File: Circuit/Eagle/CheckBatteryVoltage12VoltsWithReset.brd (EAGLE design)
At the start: 100.3 x 70 mm, 75 parts

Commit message: Aggiunte per regolazione piu precisa.
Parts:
- added E$76: W203, rcl:RTRIM3296W
- added E$77, E$79: zener 12v, ref-packages-longpad:ZDIO-7.5
- added E$78: 1k, eagle-ltspice:0204/7
- added E$80: w501, rcl:RTRIM3296W
- added E$81: zener 4.3v, ref-packages-longpad:ZDIO-7.5
- added E$82: 100, eagle-ltspice:0204/7
- E$10: value zener 12v -> zener 10v
- E$11: value 1k -> 680
- moved E$38 32.0 mm to (98.3, 67.5)
- moved E$66 29.1 mm to (98.7, 53.2)
- moved E$39 28.0 mm to (98.6, 56.6)
- moved E$67 27.0 mm to (98.4, 49.9)
- moved E$68 26.0 mm to (98.3, 60.2)
- moved E$75 24.0 mm to (98.2, 63.7)
- moved E$49 15.9 mm to (26.6, 19.2)
- moved E$10 15.9 mm to (30.9, 43.0)
- moved E$13 15.9 mm to (30.9, 46.7)
- moved E$41 15.9 mm to (26.8, 66.4)
- moved E$51 15.9 mm to (27.2, 22.9)
- moved E$55 15.9 mm to (27.2, 39.4)
- moved E$14 15.9 mm to (31.6, 58.5)
- moved E$15 15.9 mm to (31.6, 52.8)
- moved E$16 15.9 mm to (28.2, 62.6)
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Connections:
- new net S$17: E$11.2, E$76.3
- new net S$18: E$80.2, E$82.2
- new net S$19: E$81.C, E$82.1, E$9.5
- net B-1: now also E$76.2, E$81.A; no longer E$11.2
- net S$16: now also E$80.3
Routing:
- net B-1: track 93.5 -> 0.00 mm
- net S$16: track 37.6 -> 0.00 mm
- net 12V1: track 33.4 -> 0.00 mm
- net S$12: track 26.2 -> 0.00 mm
- net 0V1: track 23.6 -> 0.00 mm
- net S$13: track 17.7 -> 0.00 mm
- net S$14: track 15.8 -> 0.00 mm
- net S$7: track 14.3 -> 0.00 mm
- net S$10: track 12.7 -> 0.00 mm
- net S$8: track 12.4 -> 0.00 mm
- net S$11: track 11.2 -> 0.00 mm
- net S$5: track 10.7 -> 0.00 mm
- net S$15: track 7.93 -> 0.00 mm
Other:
- outline, holes or cut-outs redrawn

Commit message: .
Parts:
- moved E$11 0.30 mm to (44.1, 45.7)
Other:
- board text added: "Batt.+"
- board text added: "Batt.-"
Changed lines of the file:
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@@
 <layer number="25" name="tNames" color="7" fill="1" visible="no" active="yes"/>
 <layer number="26" name="bNames" color="7" fill="1" visible="no" active="yes"/>
-<layer number="27" name="tValues" color="7" fill="1" visible="no" active="yes"/>
+<layer number="27" name="tValues" color="7" fill="1" visible="yes" active="yes"/>
 <layer number="28" name="bValues" color="7" fill="1" visible="no" active="yes"/>
 <layer number="29" name="tStop" color="7" fill="3" visible="no" active="yes"/>
@@
 </text>
 <text x="39.42" y="65.785" size="0.8128" layer="22" rot="R180">Gnd</text>
-<text x="35.14" y="67.315" size="0.8128" layer="22" rot="R180">Demux
+<text x="35.44" y="65.815" size="0.8128" layer="22" rot="R180">Demux
 </text>
 <hole x="26.515" y="66.42" drill="2"/>
@@
 <text x="27.9724125" y="36.442696875" size="1.27" layer="21" rot="R180">In+</text>
 <wire x1="36.430228125" y1="22.551146875" x2="25.635228125" y2="22.551146875" width="0.254" layer="21"/>
-<text x="43.48" y="61.925" size="0.8128" layer="22">Reset
+<text x="41.98" y="63.725" size="0.8128" layer="22">Reset
 </text>
+<text x="40.8724125" y="21.442696875" size="1.27" layer="21" rot="R180">Batt.+</text>
+<text x="47.4724125" y="21.442696875" size="1.27" layer="21" rot="R180">Batt.-</text>
 </plain>
 <attributes>
@@
 <element name="E$10" library="ref-packages-longpad" library_urn="urn:adsk.eagle:library:337" package="ZDIO-7.5" value="zener 10v" x="30.935" y="42.985" smashed="yes">
 <attribute name="NAME" x="28.4458" y="44.6868" size="1.27" layer="25" ratio="10"/>
-<attribute name="VALUE" x="24.948" y="40.185" size="1.27" layer="27" ratio="10" rot="R90"/>
-</element>
-<element name="E$11" library="eagle-ltspice" package="0204/7" value="680" x="44.135" y="45.36" smashed="yes">
-<attribute name="NAME" x="41.595" y="46.6554" size="0.9906" layer="25" ratio="10"/>
-<attribute name="VALUE" x="43.1444" y="44.8774" size="0.9906" layer="27" ratio="10"/>
+<attribute name="VALUE" x="35.115" y="45.348" size="1.27" layer="27" ratio="10" rot="R180"/>
+</element>
+<element name="E$11" library="eagle-ltspice" package="0204/7" value="680" x="44.135" y="45.66" smashed="yes">
+<attribute name="NAME" x="41.595" y="46.9554" size="0.9906" layer="25" ratio="10"/>
+<attribute name="VALUE" x="43.1444" y="45.1774" size="0.9906" layer="27" ratio="10"/>
 </element>
 <element name="E$13" library="eagle-ltspice" package="0204/7" value="220" x="30.935" y="46.7" smashed="yes" rot="R180">
@@
 <element name="E$76" library="rcl" library_urn="urn:adsk.eagle:library:334" package="RTRIM3296W" package3d_urn="urn:adsk.eagle:package:26033/1" value="W203" x="52.8" y="55.5" smashed="yes" rot="R180">
 <attribute name="NAME" x="55.45" y="60" size="1.27" layer="25" rot="R270"/>
-<attribute name="VALUE" x="48.85" y="60" size="1.27" layer="27" rot="R270"/>
+<attribute name="VALUE" x="50.4" y="61.15" size="1.27" layer="27"/>
 </element>
 <element name="E$77" library="ref-packages-longpad" library_urn="urn:adsk.eagle:library:337" package="ZDIO-7.5" value="zener 12v" x="111.485" y="36.865" smashed="yes" rot="R270">
@@
 <element name="E$80" library="rcl" library_urn="urn:adsk.eagle:library:334" package="RTRIM3296W" package3d_urn="urn:adsk.eagle:package:26033/1" value="w501" x="52.2" y="24.6" smashed="yes" rot="R90">
 <attribute name="NAME" x="56.7" y="21.95" size="1.27" layer="25" rot="R180"/>
-<attribute name="VALUE" x="56.7" y="28.55" size="1.27" layer="27" rot="R180"/>
+<attribute name="VALUE" x="54.3" y="28.55" size="1.27" layer="27" rot="R180"/>
 </element>
 <element name="E$81" library="ref-packages-longpad" library_urn="urn:adsk.eagle:library:337" package="ZDIO-7.5" value="zener 4.3v" x="52.715" y="45.035" smashed="yes" rot="R90">
 <attribute name="NAME" x="51.0132" y="42.5458" size="1.27" layer="25" ratio="10" rot="R90"/>
-<attribute name="VALUE" x="55.515" y="39.048" size="1.27" layer="27" ratio="10" rot="R180"/>
+<attribute name="VALUE" x="54.852" y="48.315" size="1.27" layer="27" ratio="10" rot="R270"/>
 </element>
 <element name="E$82" library="eagle-ltspice" package="0204/7" value="100" x="52.6" y="34.235" smashed="yes" rot="R270">
@@
 <contactref element="E$9" pad="3"/>
 <contactref element="E$10" pad="A"/>
-<wire x1="42.93" y1="40.645" x2="40.325" y2="45.36" width="0" layer="19" extent="1-1"/>
-<wire x1="34.745" y1="42.985" x2="40.325" y2="45.36" width="0" layer="19" extent="1-1"/>
+<wire x1="42.93" y1="40.645" x2="40.325" y2="45.66" width="0" layer="19" extent="1-1"/>
+<wire x1="34.745" y1="42.985" x2="40.325" y2="45.66" width="0" layer="19" extent="1-1"/>
 </signal>
 <signal name="B-1">
@@
 <contactref element="E$11" pad="2"/>
 <contactref element="E$76" pad="3"/>
-<wire x1="47.945" y1="45.36" x2="52.8" y2="52.96" width="0" layer="19" extent="1-1"/>
+<wire x1="47.945" y1="45.66" x2="52.8" y2="52.96" width="0" layer="19" extent="1-1"/>
 </signal>
 <signal name="S$18">

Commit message: test di lsg
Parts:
- added E$100, E$101, E$89, E$90, E$96, E$97, E$98, E$99: (no value), wirepad:1,6/0,8
- added E$83, E$84, E$85, E$86, E$87, E$88, E$91, E$92, E$93, E$94, E$95: (no value), solpad:LSP10
- added STEP-UP-GND-OUT: (no value), wirepad:2,54/0,8
- E$50: device wirepad:2,54/0,8 -> solpad:LSP10
- moved E$50 25.5 mm to (48.0, 44.8), turned to 0 degrees
- moved E$19 4.50 mm to (44.2, 62.6)
- moved E$32 4.50 mm to (41.6, 62.6)
- moved E$65 4.50 mm to (46.7, 62.6)
- moved E$14 3.01 mm to (34.6, 58.2)
- moved E$9 1.50 mm to (44.2, 35.3)
- moved E$11 0.90 mm to (44.1, 44.8)
- moved E$63 0.30 mm to (44.5, 58.2)
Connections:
- net 0V1 renamed IN-GND-BATTERY
- net 12V1 renamed IN-12V-BATTERY
- net S$10 renamed VZ-BATTERY-LEVEL
- net S$11 renamed OUT-SERIAL-DATA
- net S$12 renamed IN-5V-FROM-NANO-SDCARD
- net S$13 renamed RESET
- net S$14 renamed IN-TO-RESET-ATTINY85
- net S$16 renamed 5.1V-STEP-UP
- net S$19 renamed VZ-ANALOG-REFERENCE
- net S$5 renamed IN-GND-NANO-SD-CARD
- net S$7 renamed TX-SERIAL-DATA
- net S$8 renamed PHOTO-DIODE
- removed net B-1: E$13.1, E$50.1, E$64.5, E$76.2, E$81.A, E$9.4
- new net STEP-UP-GND: E$13.1, E$64.5, E$76.2, E$81.A, E$9.4, STEP-UP-GND-OUT.1
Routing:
- net STEP-UP-GND: track 0.00 -> 159.1 mm
- net 5.1V-STEP-UP: track 0.00 -> 37.3 mm
- net IN-12V-BATTERY: track 0.00 -> 30.9 mm
- net IN-5V-FROM-NANO-SDCARD: track 0.00 -> 26.7 mm
- net IN-GND-BATTERY: track 0.00 -> 23.2 mm
- net RESET: track 0.00 -> 20.5 mm
- net VZ-ANALOG-REFERENCE: track 0.00 -> 20.5 mm
- net TX-SERIAL-DATA: track 0.00 -> 17.7 mm
- net IN-TO-RESET-ATTINY85: track 0.00 -> 16.4 mm
- net VZ-BATTERY-LEVEL: track 0.00 -> 13.6 mm
- net PHOTO-DIODE: track 0.00 -> 11.2 mm
- net IN-GND-NANO-SD-CARD: track 0.00 -> 10.5 mm
- net S$17: track 0.00 -> 10.2 mm
- net OUT-SERIAL-DATA: track 0.00 -> 9.82 mm
- net S$15: track 0.00 -> 8.67 mm
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
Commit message: Inizio di Modifica alla parte di reset attiny85 come da circuito corretto dopo sbaglio #3
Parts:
- added E$102: (no value), discrete:RS-2,5
- moved E$85 31.1 mm to (65.7, 43.0)
- moved E$83 22.6 mm to (62.6, 40.8)
- moved E$50 19.1 mm to (66.0, 38.3)
- moved E$88 17.2 mm to (68.5, 48.5)
- moved E$11 1.60 mm to (44.2, 46.4)
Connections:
- removed net RESET: E$64.4, E$9.1
- new net S$5: E$102.1, E$64.4, E$9.1
- net 5.1V-STEP-UP: now also E$64.5
- net STEP-UP-GND: now also E$102.2; no longer E$64.5
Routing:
- net STEP-UP-GND: track 159.1 -> 0.00 mm
- net 5.1V-STEP-UP: track 37.3 -> 0.00 mm
- net IN-12V-BATTERY: track 30.9 -> 0.00 mm
- net IN-5V-FROM-NANO-SDCARD: track 26.7 -> 0.00 mm
- net IN-GND-BATTERY: track 23.2 -> 0.00 mm
- net RESET: track 20.5 -> 0.00 mm
- net VZ-ANALOG-REFERENCE: track 20.5 -> 0.00 mm
- net TX-SERIAL-DATA: track 17.7 -> 0.00 mm
- net IN-TO-RESET-ATTINY85: track 16.4 -> 0.00 mm
- net VZ-BATTERY-LEVEL: track 13.6 -> 0.00 mm
- net PHOTO-DIODE: track 11.2 -> 0.00 mm
- net IN-GND-NANO-SD-CARD: track 10.5 -> 0.00 mm
- net S$17: track 10.2 -> 0.00 mm
- net OUT-SERIAL-DATA: track 9.82 -> 0.00 mm
- net S$15: track 8.67 -> 0.00 mm
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
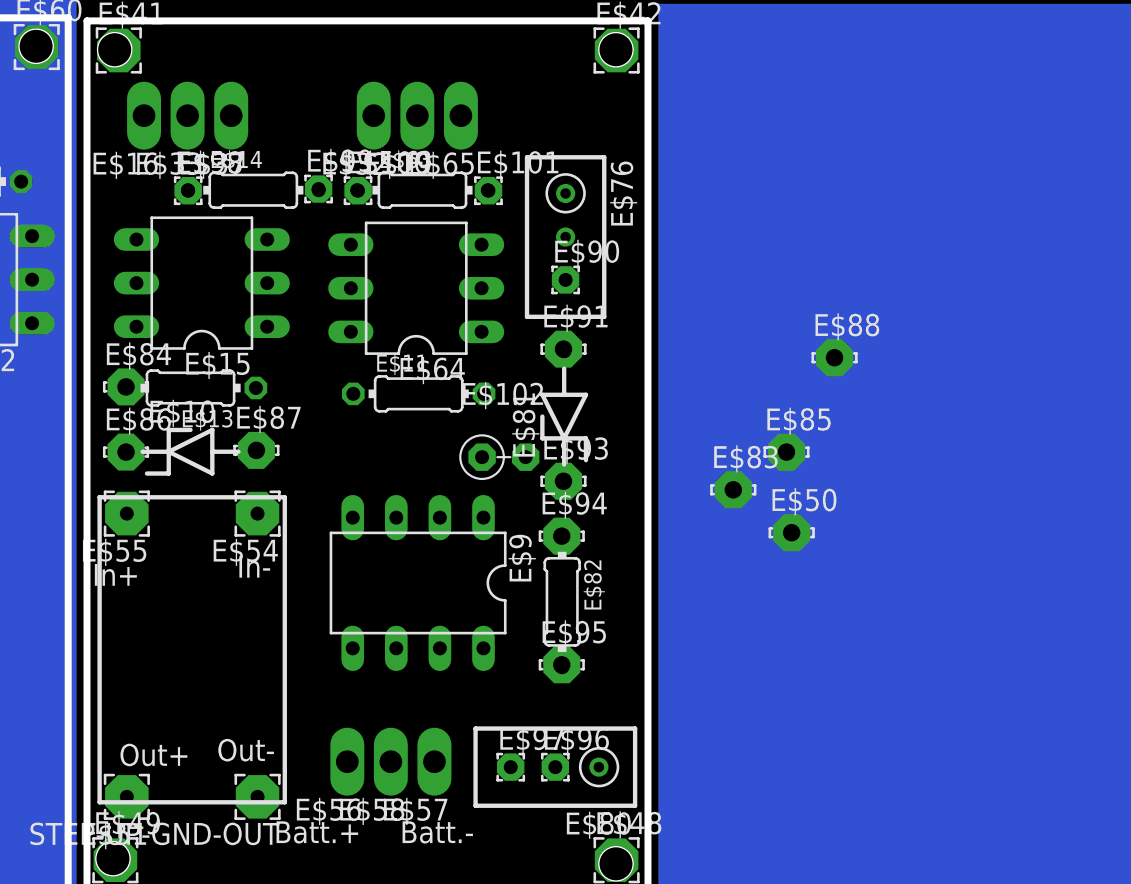
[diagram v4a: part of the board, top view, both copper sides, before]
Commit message: spostati pads pronti per una valutazione prima di portare su master   ddd
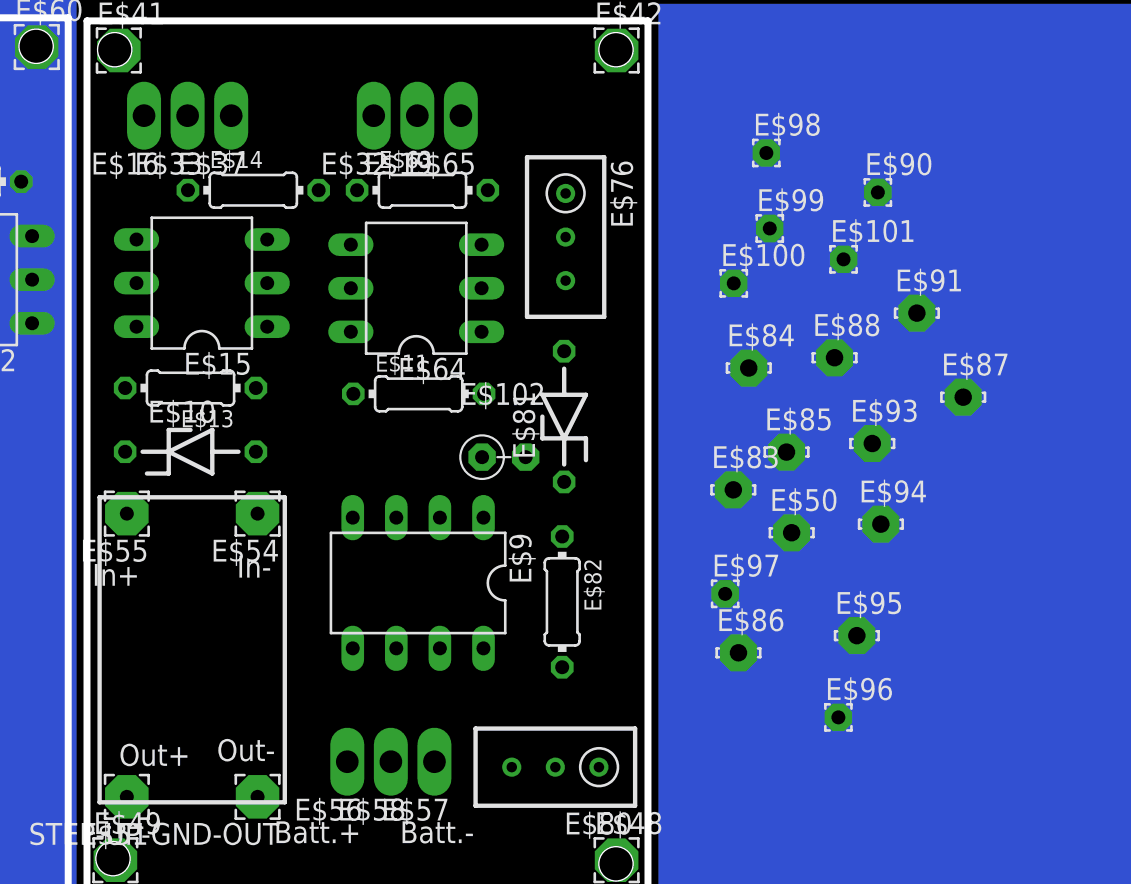
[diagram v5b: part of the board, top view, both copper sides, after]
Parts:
- moved E$87 41.3 mm to (76.0, 46.2)
- moved E$86 37.6 mm to (62.9, 31.3)
- moved E$84 36.3 mm to (63.5, 47.9)
- moved E$98 33.8 mm to (64.5, 60.4)
- moved E$99 26.4 mm to (64.7, 56.0)
- moved E$100 22.6 mm to (62.6, 52.8)
- moved E$101 21.1 mm to (69.0, 54.2)
- moved E$91 20.7 mm to (73.3, 51.1)
- moved E$90 18.9 mm to (71.0, 58.1)
- moved E$94 18.6 mm to (71.2, 38.8)
- moved E$93 18.1 mm to (70.7, 43.5)
- moved E$95 17.3 mm to (69.8, 32.3)
- moved E$96 16.8 mm to (68.7, 27.5)
- moved E$97 16.1 mm to (62.1, 34.7)

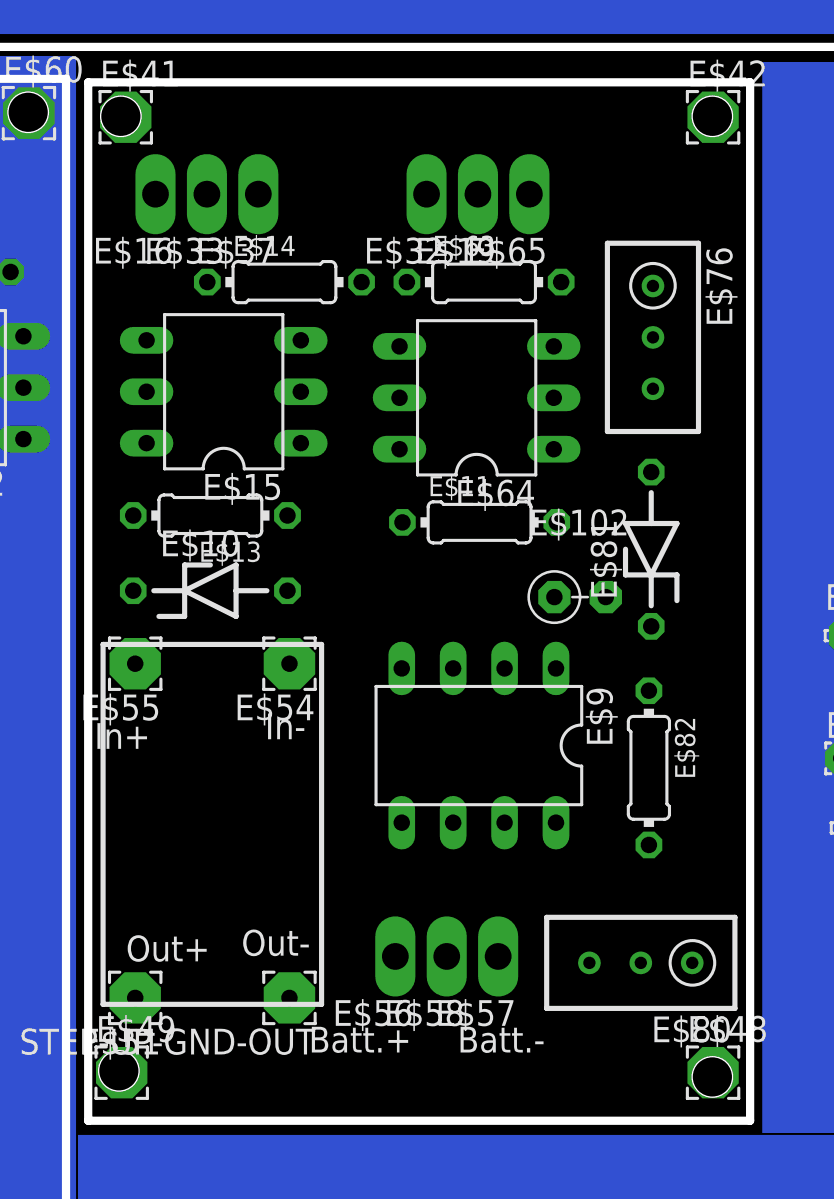
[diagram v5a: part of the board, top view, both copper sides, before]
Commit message: Modifica che deve essere controllata per verificare tutte le connessioni
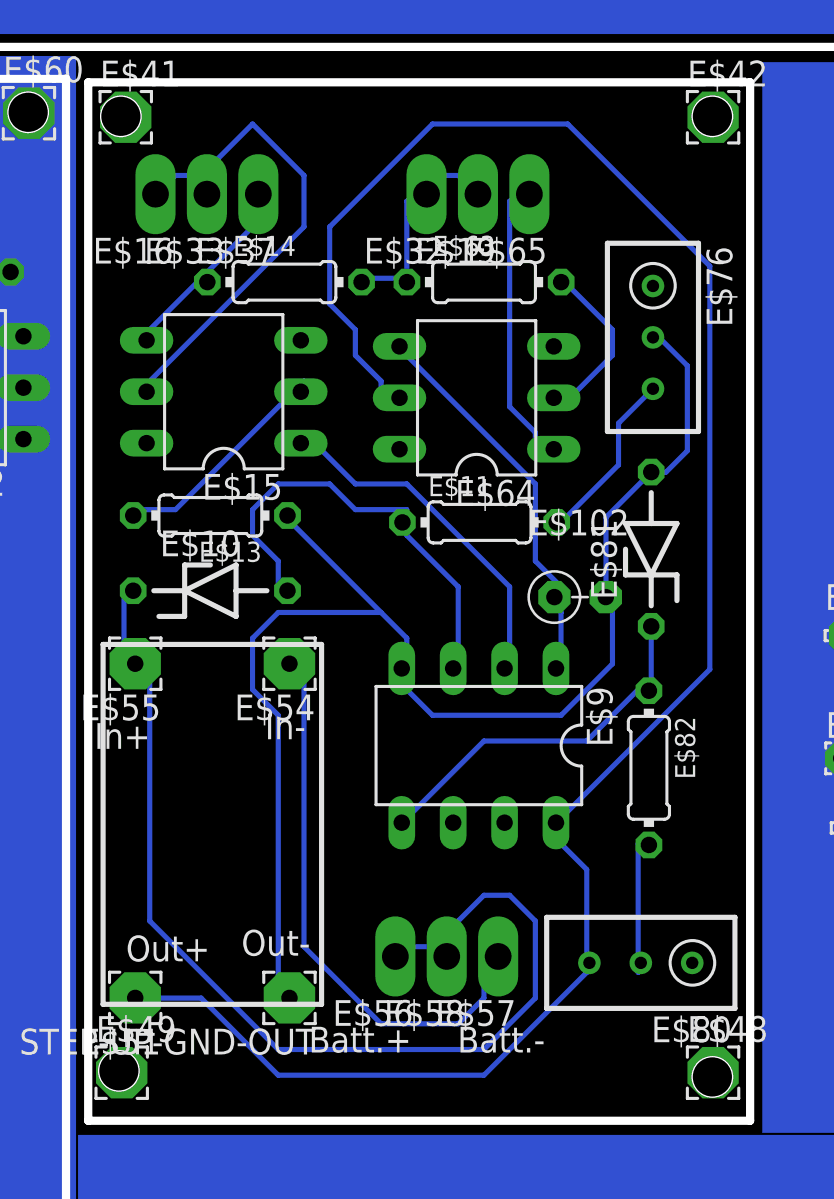
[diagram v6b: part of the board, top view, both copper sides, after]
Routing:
- net 5.1V-STEP-UP: track 0.00 -> 99.8 mm
- net STEP-UP-GND: track 0.00 -> 68.9 mm
- net IN-12V-BATTERY: track 0.00 -> 54.6 mm
- net IN-GND-BATTERY: track 0.00 -> 28.0 mm
- net IN-5V-FROM-NANO-SDCARD: track 0.00 -> 24.6 mm
- net VZ-BATTERY-LEVEL: track 0.00 -> 22.6 mm
- net S$5: track 0.00 -> 19.5 mm
- net VZ-ANALOG-REFERENCE: track 0.00 -> 18.2 mm
- net TX-SERIAL-DATA: track 0.00 -> 18.0 mm
- net IN-TO-RESET-ATTINY85: track 0.00 -> 15.3 mm
- net PHOTO-DIODE: track 0.00 -> 12.6 mm
- net IN-GND-NANO-SD-CARD: track 0.00 -> 11.5 mm
- net OUT-SERIAL-DATA: track 0.00 -> 9.81 mm
- net S$15: track 0.00 -> 9.22 mm
- net S$17: track 0.00 -> 8.70 mm
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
